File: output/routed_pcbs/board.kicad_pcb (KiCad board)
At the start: 2 copper layers, 122.3 x 101.1 mm, 39 parts

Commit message: wip
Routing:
- net P21: track 220.7 -> 183.5 mm
- net P3: track 42.2 -> 18.3 mm
- net VCC: track 52.0 -> 74.9 mm
- net P19: track 224.0 -> 212.6 mm, vias 4 -> 3
- net P6: track 148.6 -> 137.2 mm, vias 0 -> 1
- net P18: track 218.4 -> 208.0 mm, vias 4 -> 3
- net P8: track 28.5 -> 18.3 mm
- net GND: track 78.6 -> 71.2 mm
- net P20: track 171.6 -> 178.6 mm, vias 2 -> 1
- net P0: track 69.4 -> 73.3 mm, vias 0 -> 1
- net inner_home: track 25.8 -> 29.4 mm, vias 1 -> 0
- net P15: track 190.0 -> 192.6 mm, vias 4 -> 3
- net P7: track 148.3 -> 146.5 mm, vias 0 -> 1
- net P1: track 18.3 -> 19.9 mm
- net P4: track 134.6 -> 133.2 mm
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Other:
- net class Power added: clearance 0.2, trace_width 0.5, via_dia 0.8, via_drill 0.4

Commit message: Add output files
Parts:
- moved REF** 2.00 mm to (122.0, -2.20)
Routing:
- net P19: track 212.6 -> 236.9 mm
- net P18: track 208.0 -> 194.9 mm, vias 3 -> 4
- net VCC: track 74.9 -> 86.0 mm, vias 0 -> 1
- net P15: track 192.6 -> 182.3 mm
- net P4: track 133.2 -> 123.6 mm
- net P5: track 135.1 -> 140.7 mm
- net P0: track 73.3 -> 77.0 mm, vias 1 -> 2
- net P21: track 183.5 -> 180.4 mm
- net P20: track 178.6 -> 181.6 mm, vias 1 -> 2
- net GND: track 71.2 -> 70.1 mm, vias 0 -> 1
- net P7: track 146.5 -> 147.1 mm, vias 1 -> 0
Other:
- outline, holes or cut-outs redrawn

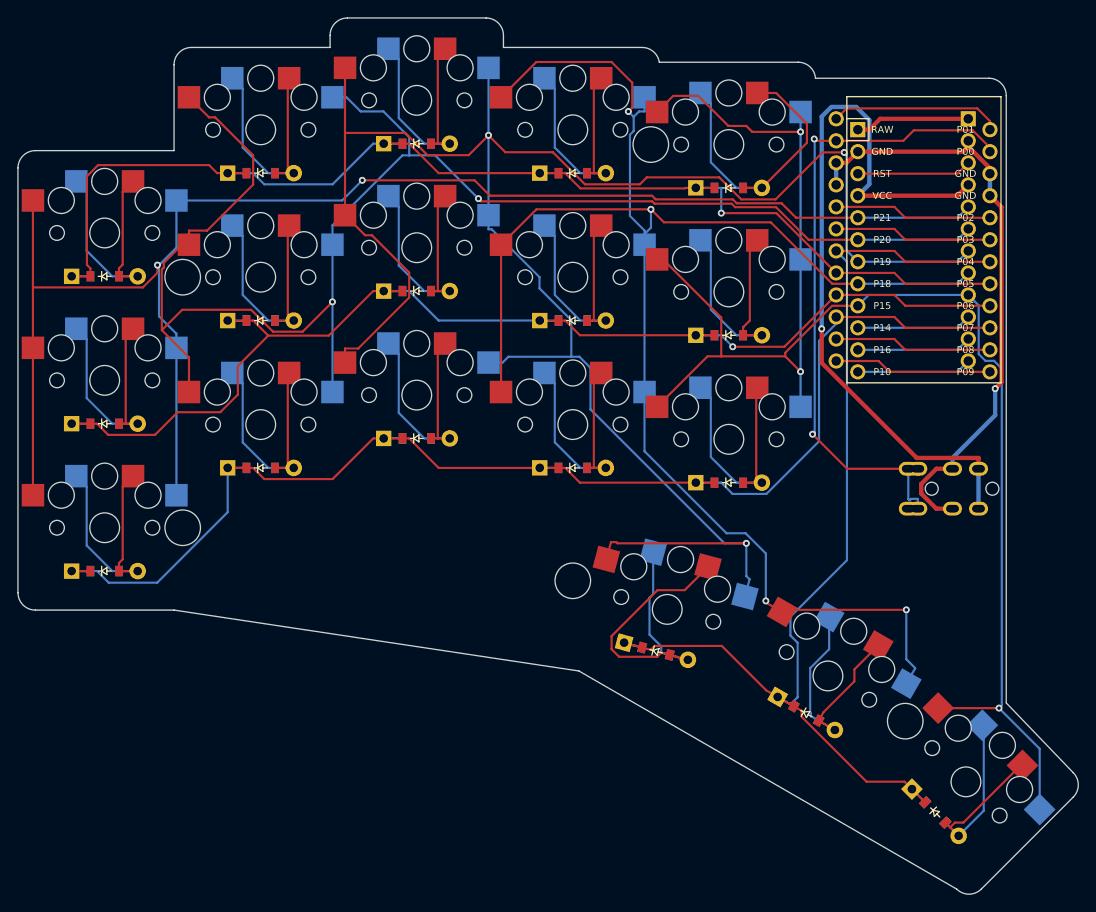
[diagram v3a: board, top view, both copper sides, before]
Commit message: Fix pinout (#3)
* Fix pin compatibility with Corne
* Add battery pins for nice!nano
* Add reset microswitch
* Fix TRRS reversibility
* Add a slider to shut off battery
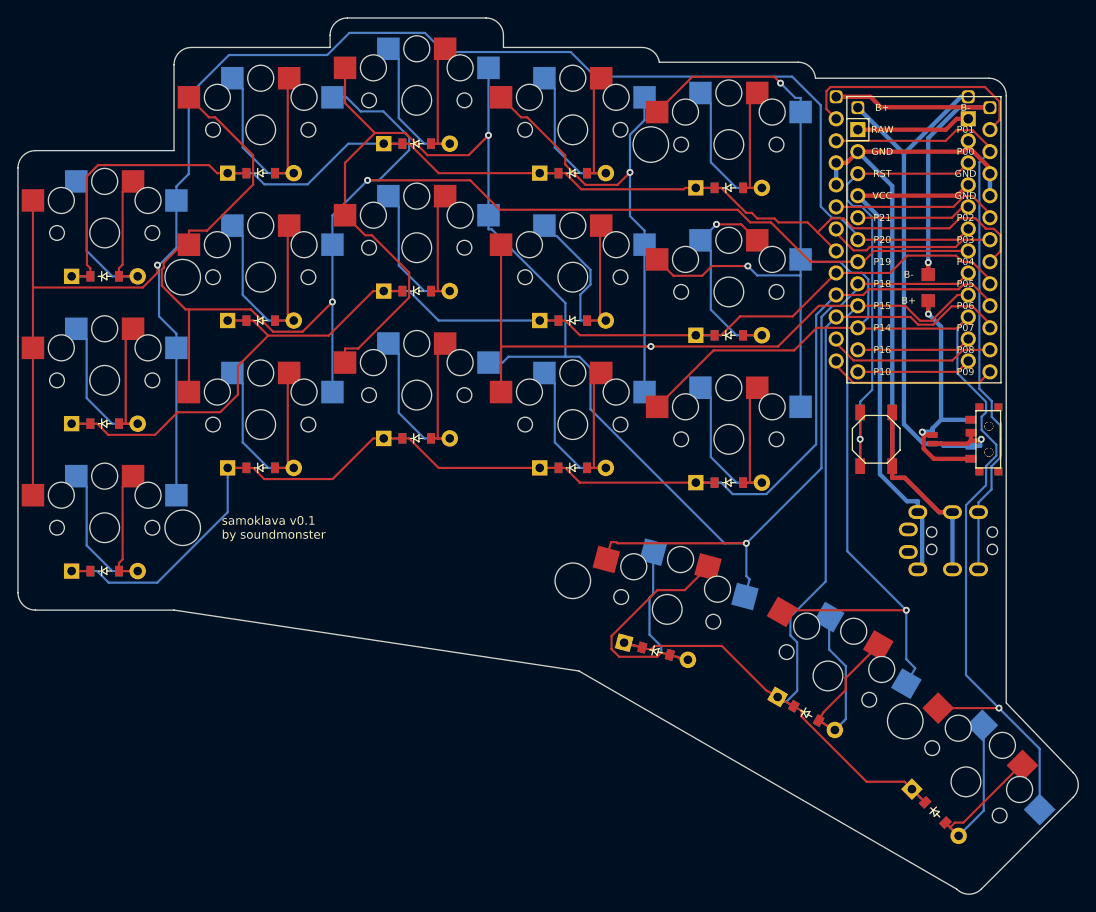
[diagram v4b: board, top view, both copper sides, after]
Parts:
- removed REF**: TRRS-PJ-320A-dual, TRRS-PJ-320A-dual
- added B1, B2: , E73:SW_TACT_ALPS_SKQGABE010, F.Cu at (107.0, -10.2)
- added J1, J2: Jumper, lib:Jumper, F.Cu at (113.5, -10.2)
- added PAD1: , SMDPad, F.Cu at (113.0, -26.2)
- added PAD2: , SMDPad, F.Cu at (113.0, -29.2)
- added T1, T2: , E73:SPDT_C128955, F.Cu at (120.0, -10.2)
- added TRRS1: TRRS-PJ-320A-dual, TRRS-PJ-320A-dual, F.Cu at (122.0, 4.80)
- added TRRS2: TRRS-PJ-320A-dual, TRRS-PJ-320A-dual, F.Cu at (122.0, 2.80)
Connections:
- D1 pad 2: P7 -> P6
- D10 pad 2: P7 -> P6
- D11 pad 2: P6 -> P5
- D12 pad 2: P5 -> P4
- D13 pad 2: P7 -> P6
- D14 pad 2: P6 -> P5
- D15 pad 2: P5 -> P4
- D16 pad 2: P4 -> P7
- D17 pad 2: P4 -> P7
- D18 pad 2: P4 -> P7
- D2 pad 2: P6 -> P5
- D3 pad 2: P5 -> P4
- D4 pad 2: P7 -> P6
- D5 pad 2: P6 -> P5
- D6 pad 2: P5 -> P4
- D7 pad 2: P7 -> P6
- D8 pad 2: P6 -> P5
- D9 pad 2: P5 -> P4
- S1 pad 2: P21 -> P20
- S10 pad 2: P18 -> P15
- S11 pad 2: P18 -> P15
- S12 pad 2: P18 -> P15
- S13 pad 2: P15 -> P14
- S14 pad 2: P15 -> P14
- S15 pad 2: P15 -> P14
- S16 pad 2: P19 -> P18
- S17 pad 2: P18 -> P15
- S18 pad 2: P15 -> P14
- S2 pad 2: P21 -> P20
- S3 pad 2: P21 -> P20
- S4 pad 2: P20 -> P19
- S5 pad 2: P20 -> P19
- S6 pad 2: P20 -> P19
- S7 pad 2: P19 -> P18
- S8 pad 2: P19 -> P18
- S9 pad 2: P19 -> P18
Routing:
- net P14: track 13.3 -> 199.7 mm, vias 0 -> 3
- net P21: track 180.4 -> 13.3 mm, vias 2 -> 0
- net Bplus: track 0.00 -> 66.2 mm, vias 0 -> 1
- net P19: track 236.9 -> 182.8 mm, vias 3 -> 2
- net Bminus: track 0.00 -> 44.0 mm, vias 0 -> 1
- net RST: track 13.3 -> 56.0 mm, vias 0 -> 1
- net Braw: track 0.00 -> 32.7 mm, vias 0 -> 2
- net P7: track 147.1 -> 117.0 mm
- net P20: track 181.6 -> 209.0 mm, vias 2 -> 1
- net GND: track 70.1 -> 96.8 mm, vias 1 -> 0
- net VCC: track 86.0 -> 60.4 mm, vias 1 -> 0
- net P4: track 123.6 -> 146.8 mm
- net P18: track 194.9 -> 211.6 mm, vias 4 -> 2
- net P6: track 137.1 -> 150.9 mm, vias 1 -> 0
- net P15: track 182.3 -> 193.2 mm
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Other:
- board text added: "samoklava v0.1 by soundmonster"
